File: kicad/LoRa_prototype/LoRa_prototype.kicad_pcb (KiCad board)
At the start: 4 copper layers, 100 x 90 mm, 138 parts, among them J1 Conn_ST_STDC14, J10 SYS, J11 BME, J12 GPS, J14 SPI_FLASH, J15 SYS, J18 MCO, J2 USB_C_Receptacle_PowerOnly_6P, J3 BAT, J4 SMA Female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

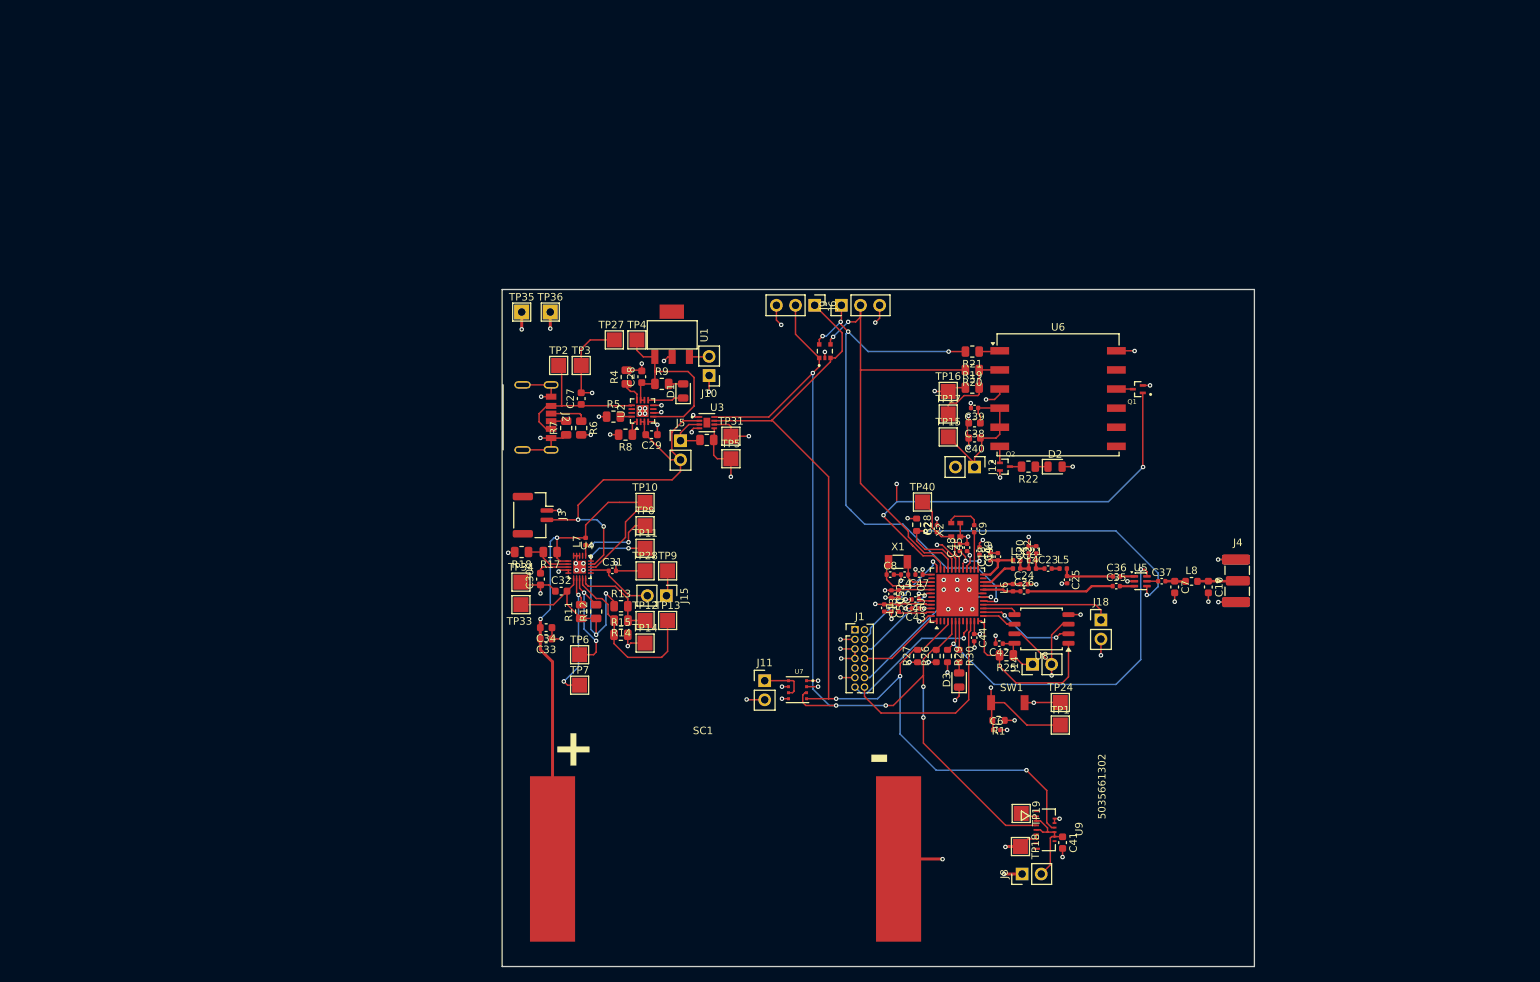
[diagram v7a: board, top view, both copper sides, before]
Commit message: Adjusted some silkscreen texts (now down to 86 DRC)
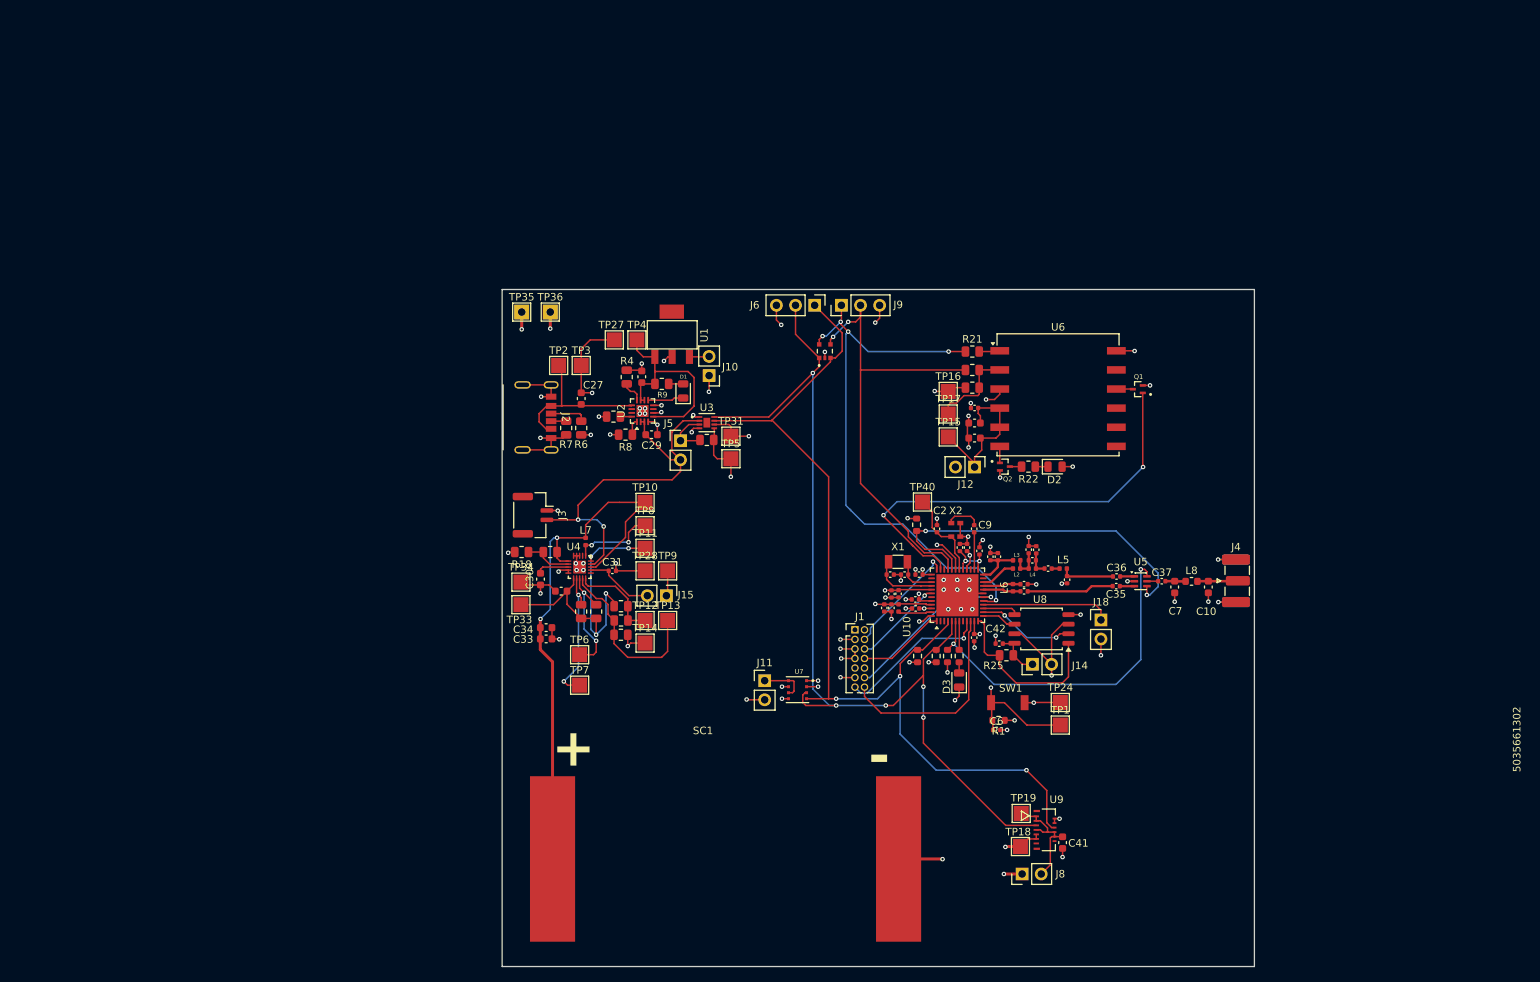
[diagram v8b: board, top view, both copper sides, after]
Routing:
- net GND: track 178.5 -> 175.8 mm, vias 88 -> 87
